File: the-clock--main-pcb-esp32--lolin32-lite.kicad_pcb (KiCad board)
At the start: 2 copper layers, 101.6 x 38.1 mm, 0 parts

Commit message: pcb session 2023-11-21T22:50:08+01:00 : almost done
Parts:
- added A1: WEMOS_LOLIN32_LITE_PHY, assemblies_uc_boards:DIP-26_900_WEMOS_LOLIN32_LITE, B.Cu at (125.7, 65.5)
- added H1: M2.5, MountingHole:MountingHole_2.7mm_M2.5, F.Cu at (54.6, 54.6)
- added H2: M2.5, MountingHole:MountingHole_2.7mm_M2.5, F.Cu at (148.6, 54.6)
- added H3: M2.5, MountingHole:MountingHole_2.7mm_M2.5, F.Cu at (148.6, 85.1)
- added H4: M2.5, MountingHole:MountingHole_2.7mm_M2.5, F.Cu at (54.6, 85.1)
- added J1: Conn_01x04, assemblies_displays_modules:TM1637_7_segments_4_digits_clock_i2c, F.Cu at (103.6, 70.0)
- added R1: 5K1, commons-passives_THT:Passive_THT_resistor_W2.54mm_L10.16mm, F.Cu at (88.9, 55.9)
- added R2: 5K1, commons-passives_THT:Passive_THT_resistor_W2.54mm_L10.16mm, F.Cu at (88.9, 58.4)
- added R3: 5K1, commons-passives_THT:Passive_THT_resistor_W2.54mm_L10.16mm, F.Cu at (88.9, 61.0)
- added R4: 5K1, commons-passives_THT:Passive_THT_resistor_W2.54mm_L10.16mm, F.Cu at (88.9, 63.5)
- added SW1: SW_Push, Button_Switch_THT:SW_PUSH_6mm_H13mm, F.Cu at (59.8, 83.0)
- added SW2: SW_Push, Button_Switch_THT:SW_PUSH_6mm_H13mm, F.Cu at (55.2, 73.2)
- added SW3: SW_Push, Button_Switch_THT:SW_PUSH_6mm_H13mm, F.Cu at (64.1, 73.2)
- added SW4: SW_Push, Button_Switch_THT:SW_PUSH_6mm_H13mm, F.Cu at (59.7, 63.2)
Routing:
- net /UP/MENU: track 0.00 -> 101.4 mm, vias 0 -> 1
- net /LEFT/-: track 0.00 -> 99.6 mm, vias 0 -> 2
- net /DOWN/BACK: track 0.00 -> 92.7 mm, vias 0 -> 1
- net /RIGHT/+: track 0.00 -> 84.8 mm, vias 0 -> 2
- net VCC: track 0.00 -> 78.2 mm, vias 0 -> 2
- net /SDA: track 0.00 -> 72.4 mm, vias 0 -> 1
- net /SCL: track 0.00 -> 69.9 mm, vias 0 -> 1
- net GND: vias 0 -> 23
- added copper zone on B.Cu, net GND
- added copper zone on F.Cu, net GND
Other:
- board text added: "https://github.com/sporniket/the-clock--main-pcb-esp32--lolin32-lite"

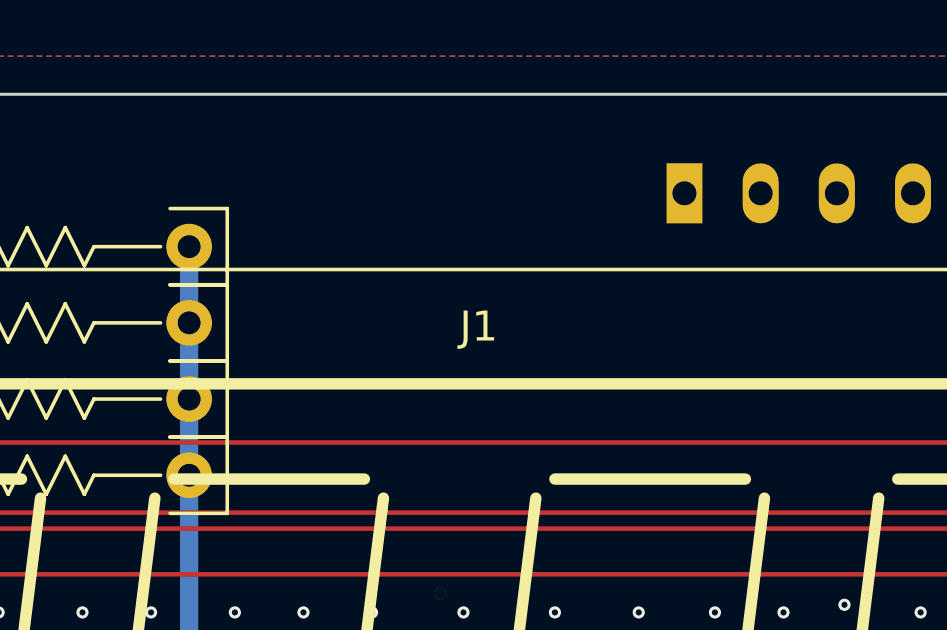
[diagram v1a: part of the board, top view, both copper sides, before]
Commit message: pcb -- added ambient light sensor
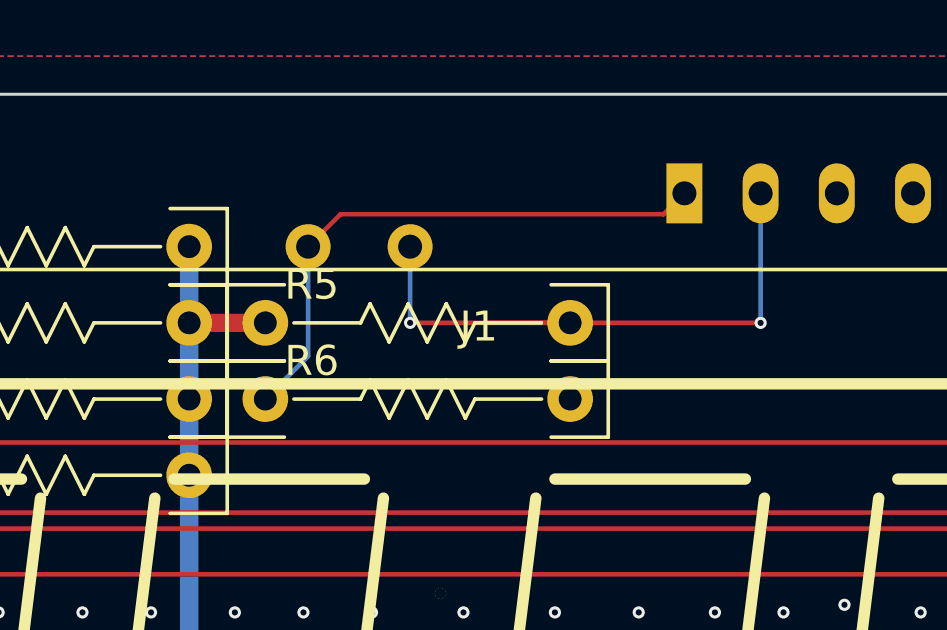
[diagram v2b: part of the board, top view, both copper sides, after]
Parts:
- added R5: 5K1, commons-passives_THT:Passive_THT_resistor_W2.54mm_L10.16mm, F.Cu at (101.6, 58.4)
- added R6: 5K1, commons-passives_THT:Passive_THT_resistor_W2.54mm_L10.16mm, F.Cu at (101.6, 61.0)
- added R7: LDR07, OptoDevice:R_LDR_5.1x4.3mm_P3.4mm_Vertical, B.Cu at (97.9, 55.9)
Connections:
- A1 pad 1: unconnected-(A1-GPIO36/VP-Pad1) -> /AMBIENT_LIGHT
- A1 pad 2: unconnected-(A1-GPIO39-Pad2) -> /AMBIENT_DARK
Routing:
- net /AMBIENT_DARK: track 0.00 -> 21.3 mm, vias 0 -> 2
- net /AMBIENT_LIGHT: track 0.00 -> 19.0 mm
- net VCC: track 78.2 -> 80.8 mm

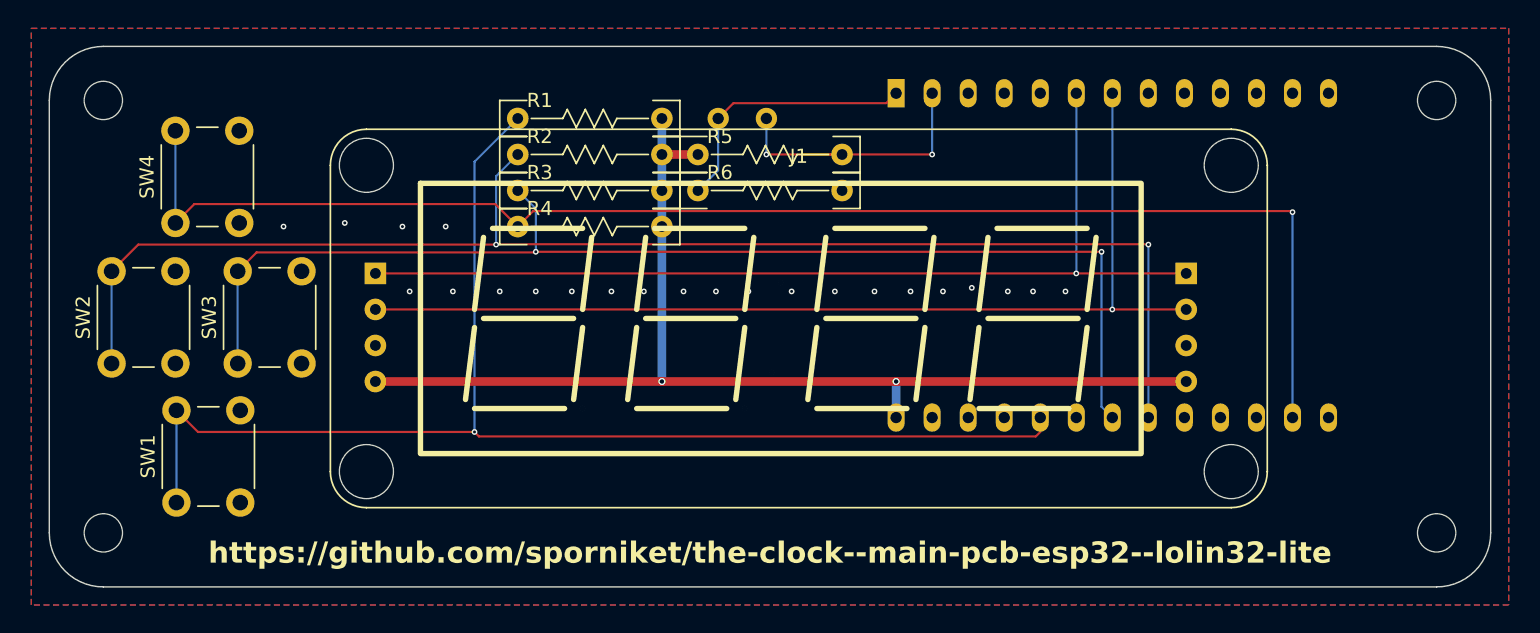
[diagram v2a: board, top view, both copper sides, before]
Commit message: finished silkscreen
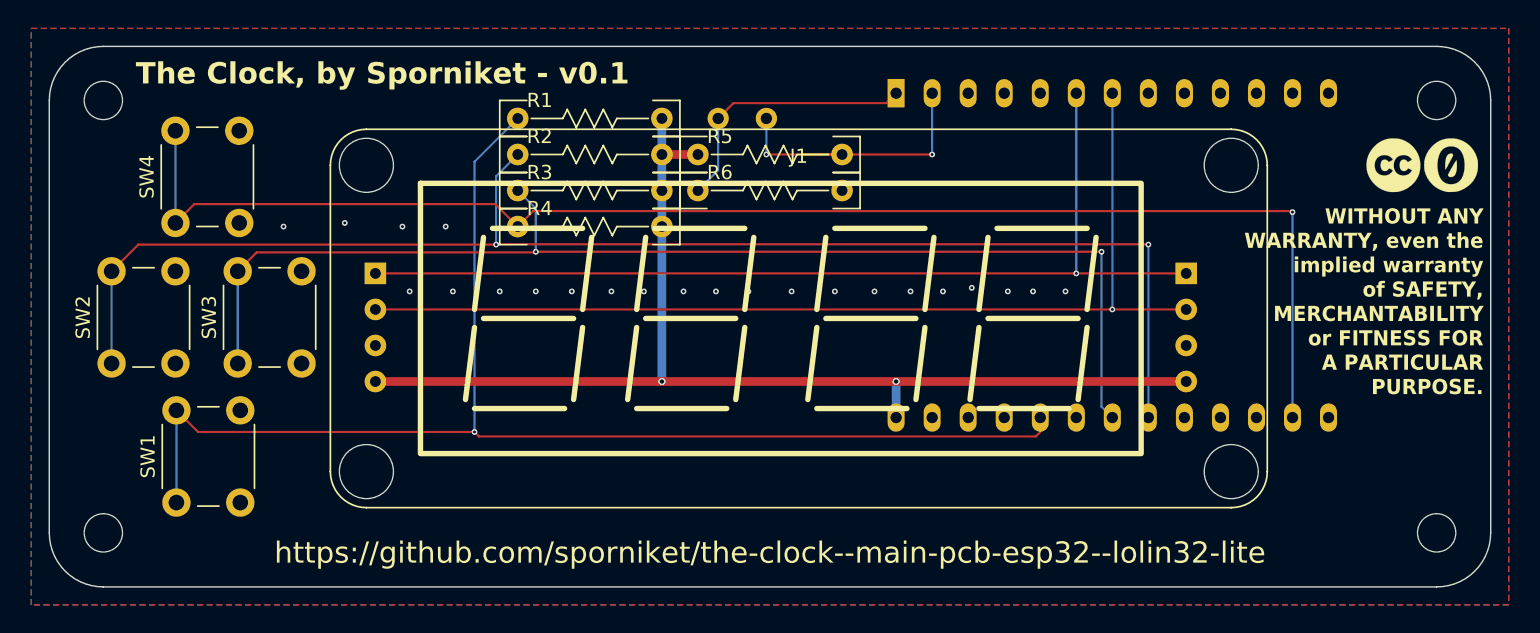
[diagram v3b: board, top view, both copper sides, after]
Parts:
- added G***: LOGO, cliparts:logo--cc--cc, F.Cu at (145.5, 59.2)
- added G***: LOGO, cliparts:logo--cc--zero, F.Cu at (149.6, 59.2)
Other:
- board text added: "The Clock, by Sporniket - v0.1"
- board text added: "WITHOUT ANY WARRANTY, even the implied warranty of SAFETY, MERCHANTABILITY or FITNESS FOR A PARTICULAR PURPOSE."
